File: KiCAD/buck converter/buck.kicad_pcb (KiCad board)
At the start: 2 copper layers, 42.2 x 24.9 mm, 16 parts, among them P1 VIN, P2 VOUT, Q1 Q_PMOS_DGS, U1 LTC1771

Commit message: Updated board layout
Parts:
- added JP1: BURST, Connectors:PINHEAD1-3, F.Cu at (113.0, 100.8)
- moved P1 6.41 mm to (113.3, 95.2)
- moved P2 1.09 mm to (113.0, 110.9)
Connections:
- U1 pad 8: +BATT -> /MODE
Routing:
- net /MODE: track 0.00 -> 19.2 mm, vias 0 -> 2
- net +BATT: track 0.00 -> 2.59 mm
- net GND: track 28.7 -> 30.2 mm
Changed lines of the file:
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@@
 (kicad_pcb (version 4) (host pcbnew 4.0.5)
   (general
-    (links 29)
+    (links 31)
     (no_connects 1)
-    (area 109.652999 88.824999 151.967001 113.867001)
+    (area 106.68 82.14614 159.00642 115.4424)
     (thickness 1.6)
     (drawings 13)
-    (tracks 65)
+    (tracks 78)
     (zones 0)
-    (modules 16)
-    (nets 11)
+    (modules 17)
+    (nets 12)
   )
   (page A4)
@@
   (net 9 /GATE)
   (net 10 /Ith)
+  (net 11 /MODE)
   (net_class Default "This is the default net class."
     (clearance 0.1524)
@@
     (uvia_drill 0.508)
     (add_net /Ith)
+    (add_net /MODE)
     (add_net /RUN/SS)
     (add_net "Net-(C2-Pad1)")
@@
   )
   (module Terminal_Blocks:TerminalBlock_Pheonix_PT-3.5mm_2pol (layer F.Cu)
-    (at 113.03 101.6 90)
+    (at 113.284 95.194 90)
     (descr "2-way 3.5mm pitch terminal block, Phoenix PT series")
     (fp_text reference P1 (at 1.75 -4.3 90) (layer F.SilkS)
@@
   )
   (module Terminal_Blocks:TerminalBlock_Pheonix_PT-3.5mm_2pol (layer F.Cu)
-    (at 113.03 109.855 90)
+    (at 113.03 110.942 90)
     (descr "2-way 3.5mm pitch terminal block, Phoenix PT series")
     (fp_text reference P2 (at 1.75 -4.3 90) (layer F.SilkS)
@@
     (tags "resistor 1206")
     (attr smd)
-    (fp_text reference R1 (at -3.937 -0.127 90) (layer F.SilkS)
+    (fp_text reference R1 (at -3.683 -0.127 90) (layer F.SilkS)
       (effects (font (size 1 1) (thickness 0.15)))
     )
@@
       (net 8 /SENSE))
     (pad 8 smd rect (at 2.7 -1.905 90) (size 1.55 0.6) (layers F.Cu F.Paste F.Mask)
+      (net 11 /MODE))
+    (model Housings_SOIC.3dshapes/SOIC-8_3.9x4.9mm_Pitch1.27mm.wrl
+      (at (xyz 0 0 0))
+      (scale (xyz 1 1 1))
+      (rotate (xyz 0 0 0))
+    )
+  )
+  (module Connectors:PINHEAD1-3 (layer F.Cu)
+    (at 113.03 100.838)
+    (fp_text reference JP1 (at -2.032 0 90) (layer F.SilkS)
+      (effects (font (size 1 1) (thickness 0.15)))
+    )
+    (fp_text value BURST (at 2.54 3.81) (layer F.Fab)
+      (effects (font (size 1 1) (thickness 0.15)))
+    )
+    (fp_line (start -1.27 -3.17) (end -1.27 3.17) (layer F.SilkS) (width 0.12))
+    (fp_line (start 6.35 -3.17) (end 6.35 3.17) (layer F.SilkS) (width 0.12))
+    (fp_line (start 6.35 -1.27) (end -1.27 -1.27) (layer F.SilkS) (width 0.12))
+    (fp_line (start -1.27 -3.17) (end 6.35 -3.17) (layer F.SilkS) (width 0.12))
+    (fp_line (start 6.35 3.17) (end -1.27 3.17) (layer F.SilkS) (width 0.12))
+    (fp_line (start -1.52 -3.42) (end 6.6 -3.42) (layer F.CrtYd) (width 0.05))
+    (fp_line (start -1.52 -3.42) (end -1.52 3.42) (layer F.CrtYd) (width 0.05))
+    (fp_line (start 6.6 3.42) (end 6.6 -3.42) (layer F.CrtYd) (width 0.05))
+    (fp_line (start 6.6 3.42) (end -1.52 3.42) (layer F.CrtYd) (width 0.05))
+    (pad 1 thru_hole oval (at 0 0) (size 1.51 3.01) (drill 1) (layers *.Cu *.Mask)
+      (net 1 GND))
+    (pad 2 thru_hole oval (at 2.54 0) (size 1.51 3.01) (drill 1) (layers *.Cu *.Mask)
+      (net 11 /MODE))
+    (pad 3 thru_hole oval (at 5.08 0) (size 1.51 3.01) (drill 1) (layers *.Cu *.Mask)
       (net 5 +BATT))
-    (model Housings_SOIC.3dshapes/SOIC-8_3.9x4.9mm_Pitch1.27mm.wrl
-      (at (xyz 0 0 0))
-      (scale (xyz 1 1 1))
-      (rotate (xyz 0 0 0))
-    )
-  )
-  (gr_text - (at 118.364 97.028 90) (layer F.SilkS)
+  )
+  (gr_text - (at 118.618 94.996 90) (layer F.SilkS)
     (effects (font (size 0.8128 0.8128) (thickness 0.0762)))
   )
@@
     (effects (font (size 0.8128 0.8128) (thickness 0.0762)))
   )
-  (gr_text + (at 118.364 102.616) (layer F.SilkS)
+  (gr_text + (at 118.618 100.584) (layer F.SilkS)
     (effects (font (size 0.8128 0.8128) (thickness 0.0762)))
   )
@@
   (gr_line (start 109.728 88.9) (end 150.876 88.9) (layer Edge.Cuts) (width 0.15))
   (gr_line (start 109.728 113.284) (end 109.728 88.9) (layer Edge.Cuts) (width 0.15))
+  (segment (start 113.03 107.442) (end 113.03 105.744944) (width 1.016) (layer F.Cu) (net 1))
+  (segment (start 113.03 105.744944) (end 113.872944 104.902) (width 1.016) (layer F.Cu) (net 1))
+  (segment (start 113.872944 104.902) (end 114.483 104.902) (width 1.016) (layer F.Cu) (net 1))
   (segment (start 121.285 111.92) (end 119.22 111.92) (width 1.016) (layer F.Cu) (net 1))
   (segment (start 119.22 111.92) (end 119.126 112.014) (width 1.016) (layer F.Cu) (net 1))
   (via (at 119.126 112.014) (size 0.6858) (drill 0.3302) (layers F.Cu B.Cu) (net 1))
   (segment (start 121.432 104.902) (end 114.483 104.902) (width 1.016) (layer F.Cu) (net 1))
-  (segment (start 114.483 104.902) (end 113.03 106.355) (width 1.016) (layer F.Cu) (net 1))
   (segment (start 138.43 111.085) (end 138.009 111.506) (width 1.016) (layer F.Cu) (net 1))
   (segment (start 138.009 111.506) (end 129.794 111.506) (width 1.016) (layer F.Cu) (net 1))
@@
   (segment (start 121.365 109.14) (end 121.285 109.22) (width 0.1524) (layer F.Cu) (net 4))
   (segment (start 131.445 104.2274) (end 131.445 103.665) (width 0.1524) (layer F.Cu) (net 4))
+  (segment (start 121.825 102.235) (end 121.825 99.81) (width 1.016) (layer F.Cu) (net 5))
+  (segment (start 121.825 99.81) (end 121.94 99.695) (width 1.016) (layer F.Cu) (net 5))
   (segment (start 133.35 93.726) (end 133.35 94.22) (width 0.508) (layer F.Cu) (net 6))
   (segment (start 133.35 94.22) (end 133.27 94.3) (width 0.508) (layer F.Cu) (net 6))
@@
   (segment (start 132.48 100.885) (end 130.175 103.19) (width 0.1524) (layer F.Cu) (net 10))
   (segment (start 130.175 103.19) (end 130.175 103.665) (width 0.1524) (layer F.Cu) (net 10))
+  (segment (start 129.032 100.584) (end 129.032 98.392) (width 0.1524) (layer F.Cu) (net 11))
+  (segment (start 129.032 98.392) (end 128.905 98.265) (width 0.1524) (layer F.Cu) (net 11))
+  (segment (start 116.332 98.044) (end 117.457034 98.044) (width 0.1524) (layer B.Cu) (net 11))
+  (via (at 129.032 100.584) (size 0.6858) (drill 0.3302) (layers F.Cu B.Cu) (net 11))
+  (segment (start 117.457034 98.044) (end 119.997034 100.584) (width 0.1524) (layer B.Cu) (net 11))
+  (segment (start 119.997034 100.584) (end 129.032 100.584) (width 0.1524) (layer B.Cu) (net 11))
+  (segment (start 115.57 100.838) (end 115.57 98.806) (width 0.1524) (layer F.Cu) (net 11))
+  (segment (start 115.57 98.806) (end 116.332 98.044) (width 0.1524) (layer F.Cu) (net 11))
+  (via (at 116.332 98.044) (size 0.6858) (drill 0.3302) (layers F.Cu B.Cu) (net 11))
   (zone (net 5) (net_name +BATT) (layer F.Cu) (hatch edge 0.508)
     (connect_pads (clearance 0.508))

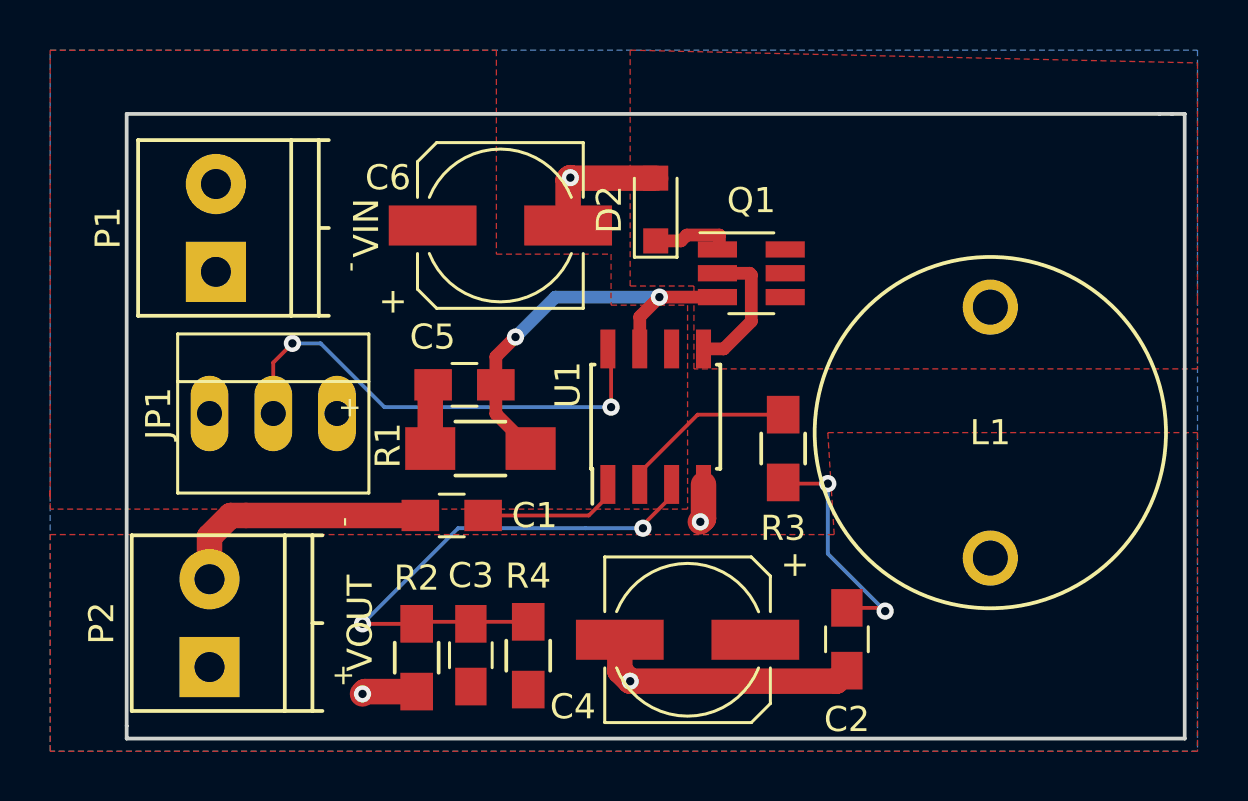
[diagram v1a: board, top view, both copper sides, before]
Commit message: Updated inductor footprint
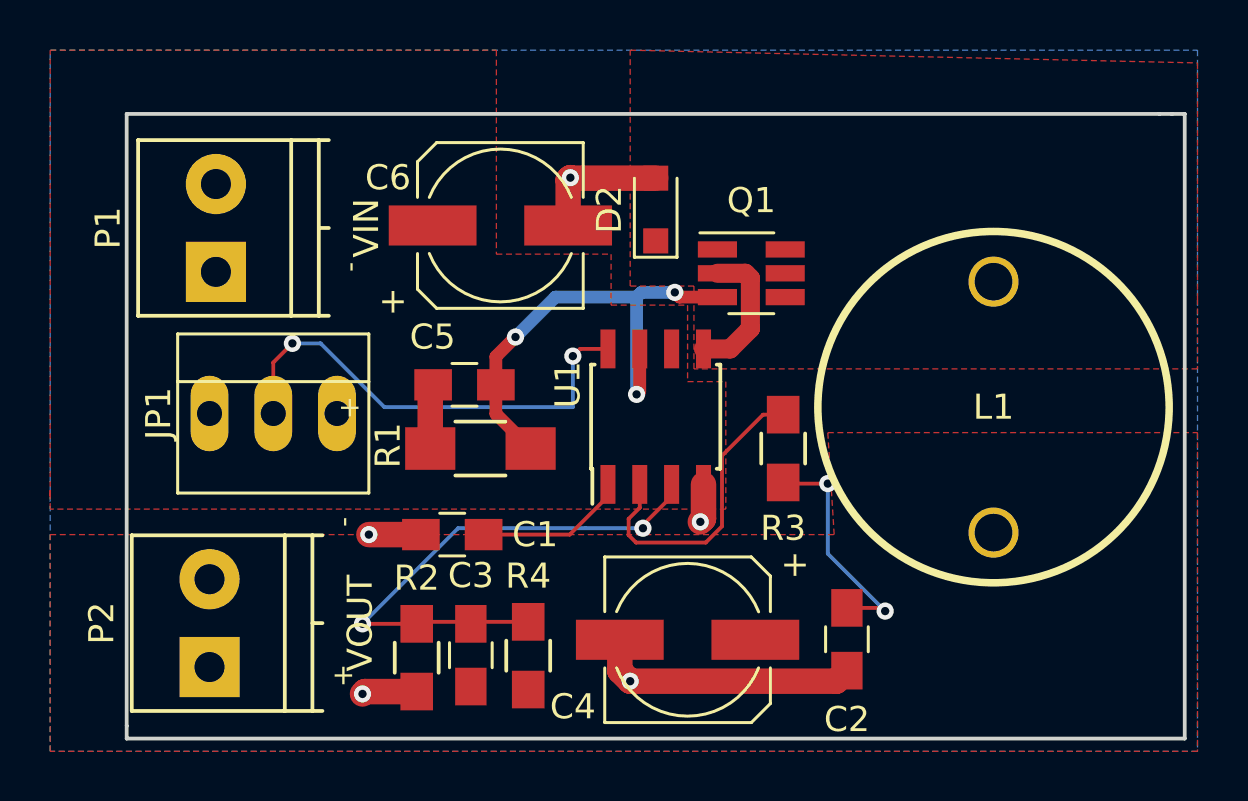
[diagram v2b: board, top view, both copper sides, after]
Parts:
- L1: footprint Buck:inductor_th_10mm -> Buck:14mm-Inductor
- moved L1 1.02 mm to (144.3, 100.6)
- moved C1 0.76 mm to (122.7, 105.7)
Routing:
- net GND: track 30.2 -> 21.8 mm, vias 4 -> 5
- net /Ith: track 7.14 -> 12.7 mm
- net /SENSE: track 16.4 -> 19.9 mm, vias 2 -> 3
- net /Vsw: track 3.24 -> 0.00 mm
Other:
- net class Gate added: clearance 0.1524, trace_width 0.762, via_dia 0.6858, via_drill 0.3302
